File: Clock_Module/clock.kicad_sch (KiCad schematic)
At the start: 28 parts, among them SW1 Switch, U1 74LS08, U2 74LS32, U3 74LS04, U4 LM555xN, U5 LM555xN, U6 LM555xN

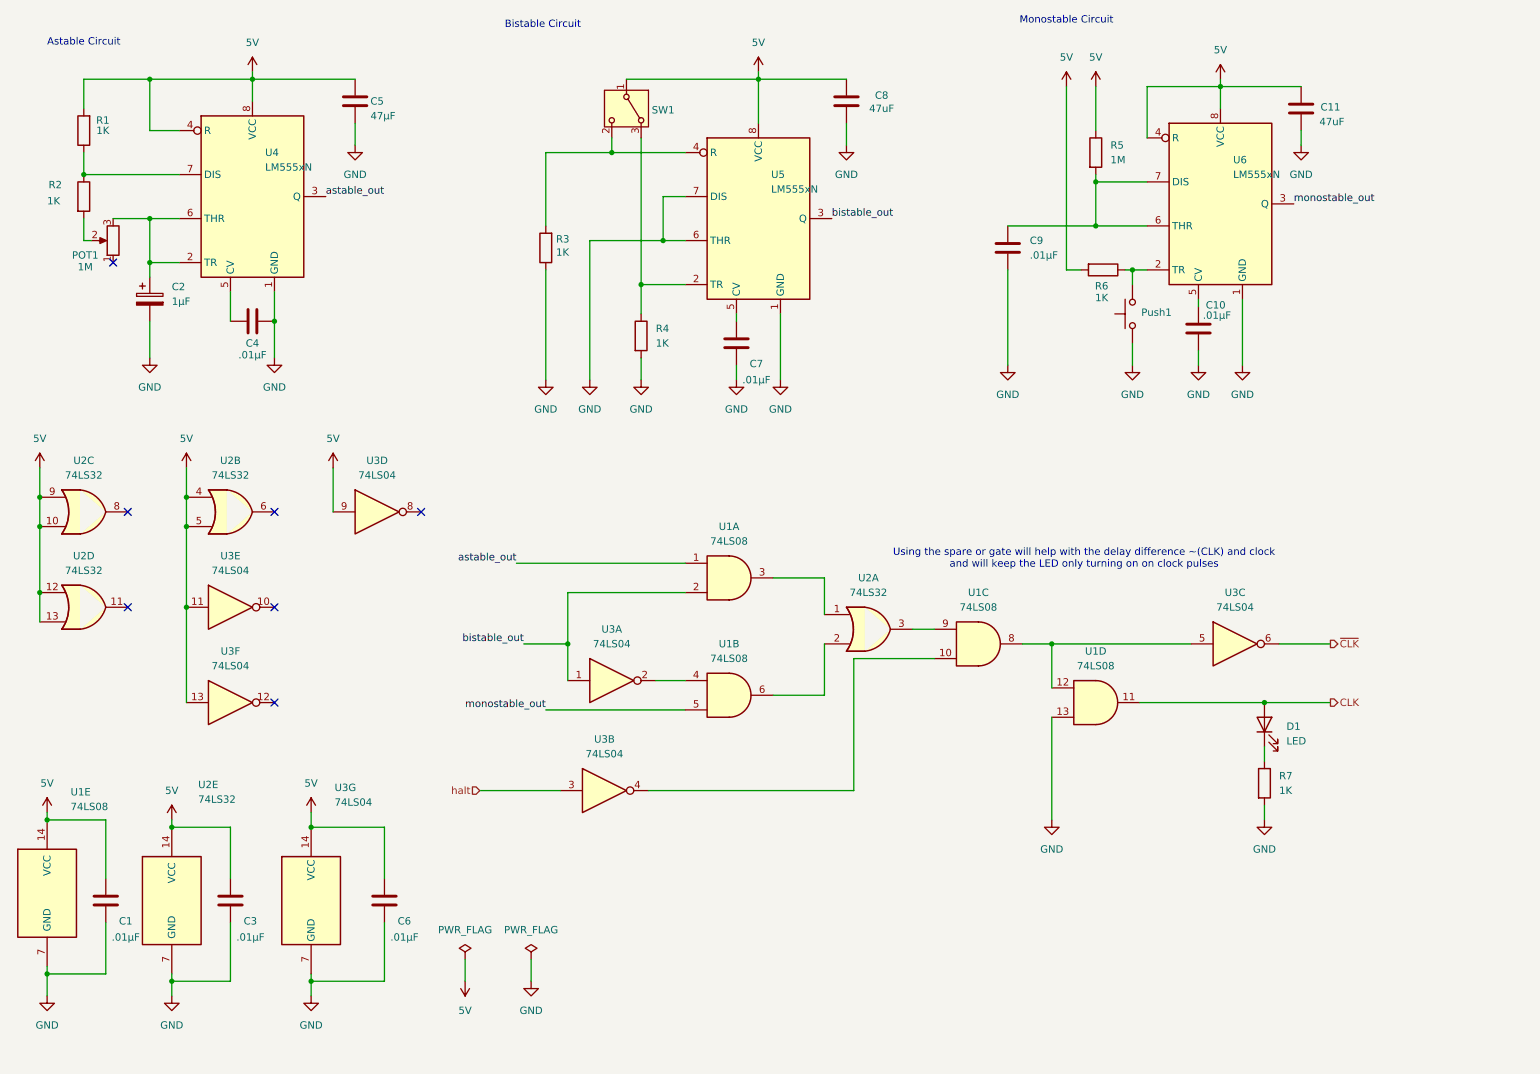
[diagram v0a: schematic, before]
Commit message: Updated Clock Module Schematic, and moved Instruction Register to new board
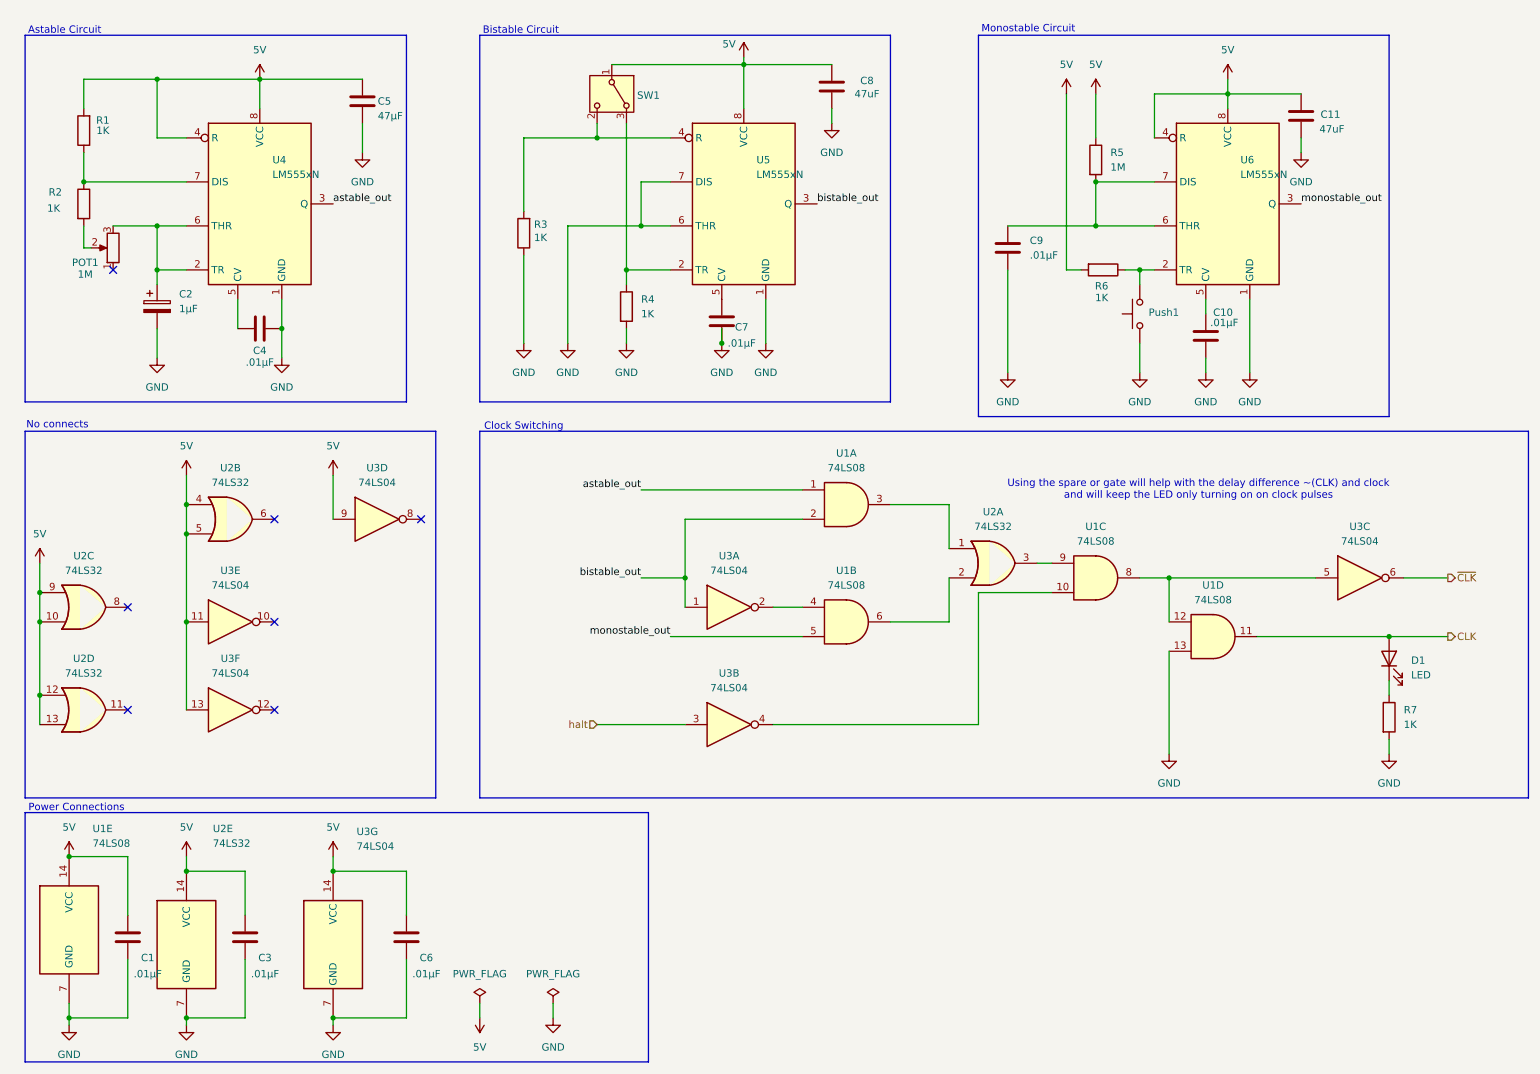
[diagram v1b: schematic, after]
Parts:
- POT1: footprint Potentiometer_THT:Potentiometer_Bourns_3386F_Vertical -> Potentiometer_THT:Potentiometer_Bourns_3266Y_Vertical
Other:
- note added: "Clock Switching"
- note added: "No connects"
- note added: "Power Connections"
- company: (none) -> Arsenal Gear
- title: (none) -> Clock Logic
- moved on the sheet: C1, C10, C11, C2, C3, C4, C5, C6, C7, C8, D1, POT1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

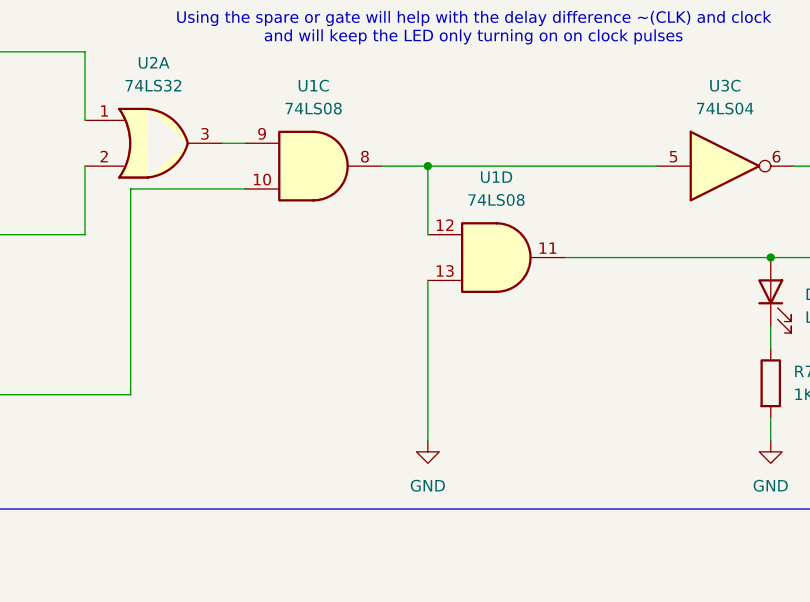
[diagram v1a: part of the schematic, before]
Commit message: mostly routed IR, fixed logic issue in Clock Module
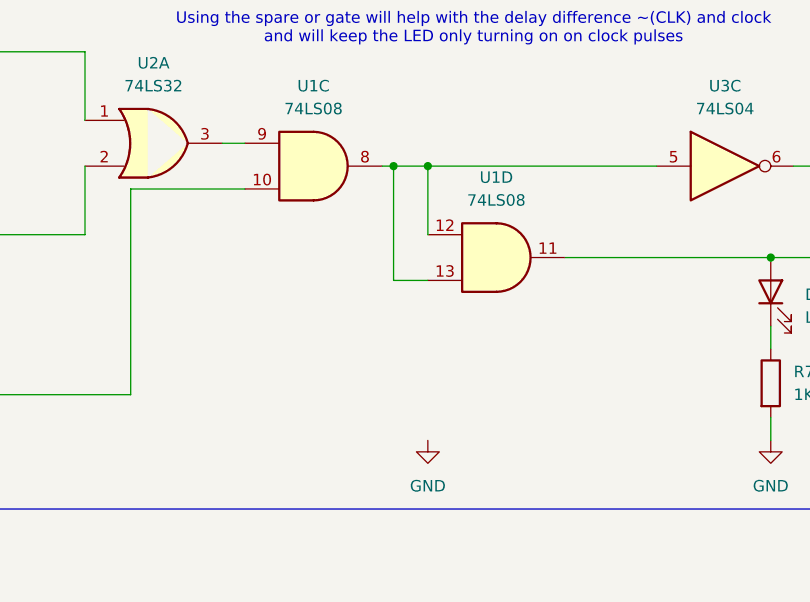
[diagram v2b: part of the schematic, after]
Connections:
- net GND: no longer U1.13
- net at U1.12, U1.8, U3.5: now also U1.13
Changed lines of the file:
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@@
+		(color 0 0 0 0)
+	)
+	(junction
+		(at 214.63 111.76)
+		(diameter 0)
 		(color 0 0 0 0)
 	)
@@
 	(wire
 		(pts
+			(xy 218.44 124.46) (xy 214.63 124.46)
+		)
+		(stroke
+			(width 0)
+			(type default)
+		)
+	)
+	(wire
+		(pts
 			(xy 121.92 22.86) (xy 144.78 22.86)
 		)
@@
 	(wire
 		(pts
-			(xy 218.44 111.76) (xy 213.36 111.76)
+			(xy 218.44 111.76) (xy 214.63 111.76)
+		)
+		(stroke
+			(width 0)
+			(type default)
+		)
+	)
+	(wire
+		(pts
+			(xy 214.63 111.76) (xy 213.36 111.76)
 		)
 		(stroke
@@
 	(wire
 		(pts
+			(xy 214.63 124.46) (xy 214.63 111.76)
+		)
+		(stroke
+			(width 0)
+			(type default)
+		)
+	)
+	(wire
+		(pts
 			(xy 213.36 58.42) (xy 215.9 58.42)
 		)
@@
 		)
 		(stroke
-			(width 0)
-			(type default)
-		)
-	)
-	(wire
-		(pts
-			(xy 218.44 124.46) (xy 218.44 142.24)
-		)
-		(stroke

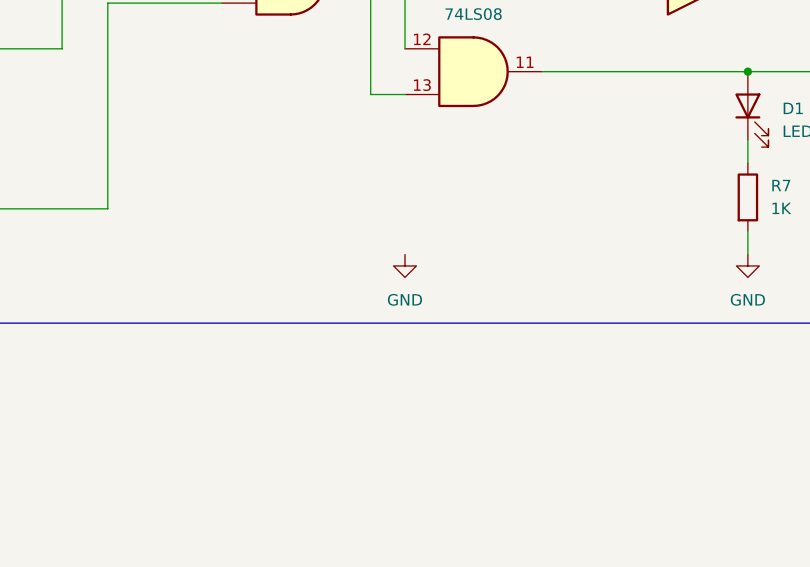
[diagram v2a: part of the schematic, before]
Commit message: fixed clock module, made it back into pc104 board standard
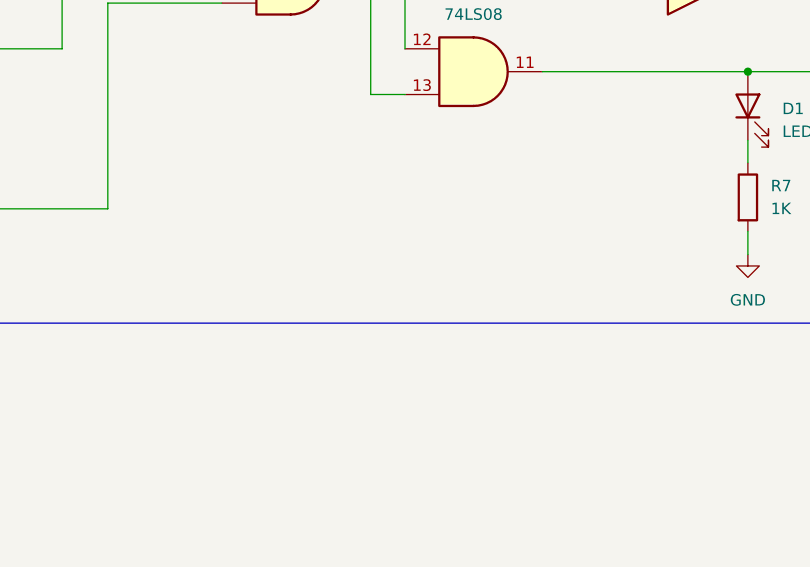
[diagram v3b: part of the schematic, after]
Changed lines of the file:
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@@
-	(symbol
-		(lib_id "power:GND")
-		(at 218.44 142.24 0)
-		(unit 1)
-		(exclude_from_sim yes)
-		(in_bom yes)
-		(on_board yes)
-		(dnp no)
-		(fields_autoplaced yes)
-		(property "Reference" "#PWR024"
-			(at 218.44 148.59 0)
-			(effects
-				(font
-					(size 1.27 1.27)
-				)
-				(hide yes)
-			)
-		)
-		(property "Value" "GND"
-			(at 218.44 147.32 0)
-			(effects
-				(font
-					(size 1.27 1.27)
-				)
-			)
-		)
-		(property "Footprint" ""
-			(at 218.44 142.24 0)
-			(effects
-				(font
-					(size 1.27 1.27)
-				)
-				(hide yes)
-			)
-		)
-		(property "Datasheet" ""
-			(at 218.44 142.24 0)
-			(effects
-				(font
-					(size 1.27 1.27)
-				)
-				(hide yes)
-			)
-		)
-		(property "Description" "Power symbol creates a global label with name \"GND\" , ground"
-			(at 218.44 142.24 0)
-			(effects
-				(font
-					(size 1.27 1.27)
-				)
-				(hide yes)
-			)
-		)
-		(pin "1"
-		)
-		(instances
-			(project "Clock_Module"
-				(path "/e63e39d7-6ac0-4ffd-8aa3-1841a4541b55/b59c88d4-28ff-4eb7-828e-811871f60e03"
-					(reference "#PWR024")
-					(unit 1)
-				)
-			)
-		)
-	)
 	(symbol
 		(lib_id "power:GND")
